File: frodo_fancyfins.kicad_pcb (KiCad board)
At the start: 2 copper layers, 150 x 230 mm, 116 parts, among them J1 Molex MicroFit 2x3, J2 Molex MicroFit 2x3, J3 U.FL, J4 SWD Header, Q1 AO3400A, U10 L78L05_SOT89, U11 L78L05_SOT89, U12 L78L05_SOT89, U14 INA826, U15 AZ1117-5.0, U16 AZ1117-5.0, U17 W25Q128JVP, U18 AS321KTR-G1, U19 INA826, U2 MCP2562-E-SN, U3 AZ1117-3.3, U4 STM32F103RCTx, U5 L78L05_SOT89, U6 L78L05_SOT89, U7 L78L05_SOT89, U8 L78L05_SOT89, U9 L78L05_SOT89, Y1 8MHz 12pF

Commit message: PCB Layout (traces, edge cuts, silk screen, 3d models)
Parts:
- J1: moved to B.Cu
- J2: moved to F.Cu
- moved J2 14.0 mm to (36.0, 287.5), turned to 0 degrees
- moved J1 12.4 mm to (36.0, 301.5), turned to 0 degrees
- moved R15 10.9 mm to (129.4, 197.7)
- moved R14 10.9 mm to (129.4, 200.2)
- moved U18 10.9 mm to (132.7, 199.4)
- moved J4 9.71 mm to (36.7, 307.5)
- moved R2 9.10 mm to (89.0, 220.6), turned to 0 degrees
- moved U17 6.51 mm to (95.5, 204.7), turned to 180 degrees
- moved C43 5.86 mm to (90.5, 207.2), turned to 90 degrees
- moved C13 2.00 mm to (69.0, 207.0)
- moved C14 2.00 mm to (69.0, 203.0)
- moved C39 2.00 mm to (52.0, 207.0)
- moved C40 2.00 mm to (52.0, 211.0)
- moved C41 2.00 mm to (52.0, 215.0)
- moved C42 2.00 mm to (52.0, 203.0)
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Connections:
- J4 pad 1: +3V3 -> +3.3V
- U2 pad 5: +3V3 -> +3.3V
- U4 pad 14: VDsense -> unconnected-(U4-PA0-Pad14)
- U4 pad 17: unconnected-(U4-PA3-Pad17) -> DIO1_RADIO
- U4 pad 20: SPI_CS_RADIO -> DIO3_RADIO
- U4 pad 24: unconnected-(U4-PC4-Pad24) -> SPI_CS_RADIO
- U4 pad 27: unconnected-(U4-PB1-Pad27) -> VDsense
- U4 pad 33: SPI_CS_FLASH -> unconnected-(U4-PB12-Pad33)
- U4 pad 37: unconnected-(U4-PC6-Pad37) -> SPI_CS_FLASH
- U4 pad 51: DIO1_RADIO -> unconnected-(U4-PC10-Pad51)
- U4 pad 52: DIO3_RADIO -> unconnected-(U4-PC11-Pad52)
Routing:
- net +3.3VA: track 0.00 -> 582.7 mm, vias 0 -> 8
- net /strain_gauge0/SG_GND: track 0.00 -> 394.3 mm
- net +3.3V: track 0.00 -> 357.5 mm, vias 0 -> 10
- net GND: track 4.00 -> 319.5 mm, vias 0 -> 267
- net VD: track 0.00 -> 259.2 mm
- net CAN-: track 0.00 -> 240.1 mm
- net CAN+: track 0.00 -> 232.4 mm, vias 0 -> 2
- net SG_REF: track 0.00 -> 231.0 mm, vias 0 -> 3
- net LED_Signal: track 0.00 -> 214.8 mm, vias 0 -> 4
- net VDC: track 0.00 -> 206.8 mm
- net +VSW: track 0.00 -> 164.8 mm
- net SWDIO: track 0.00 -> 157.2 mm
- net SWCLK: track 0.00 -> 151.1 mm
- net VDsense: track 0.00 -> 133.4 mm
- net SG_VOUT0: track 0.00 -> 130.8 mm, vias 0 -> 2
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- added copper zone on B.Cu, net +VSW
- added copper zone on B.Cu, net VDC
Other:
- board size 150 x 230 mm -> 170 x 240 mm

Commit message: Minor changes for ordering
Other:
- outline, holes or cut-outs redrawn
- board text added: "FRoDO Fancy Fins"
- board text added: "JLCJLCJLCJLC"
- board text added: "rev 0"
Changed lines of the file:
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@@
         (effects (font (size 1 1) (thickness 0.15)))
     )
-    (fp_text value "SWD Header" (at 0 9.95 90) (layer "F.Fab")
+    (fp_text value "SWD Header" (at 0 9.95 90) (layer "F.Fab") hide
         (effects (font (size 1 1) (thickness 0.15)))
     )
-    (fp_text user "${REFERENCE}" (at 0 3.81) (layer "F.Fab")
+    (fp_text user "${REFERENCE}" (at 0 3.81) (layer "F.Fab") hide
         (effects (font (size 1 1) (thickness 0.15)))
     )
@@
   (gr_line (start 50.5 309.5) (end 50.5 80.5)
     (stroke (width 0.15) (type dash)) (layer "F.SilkS"))
-  (gr_poly locked
+  (gr_poly
     (pts
       (xy 50 70)
@@
       (xy 48.5 70)
       (xy 35 70)
-      (xy 35 260)
-      (xy 30 270)
+      (xy 35 270)
+      (xy 30 280)
       (xy 30 310)
       (xy 50 310)
@@
     )
     (stroke (width 0.2) (type solid)) (fill none) (layer "Edge.Cuts"))
+  (gr_text "JLCJLCJLCJLC" (at 41.3 256.3 90) (layer "F.SilkS")
+    (effects (font (size 1 1) (thickness 0.15)) (justify left bottom))
+  )
+  (gr_text "rev 0\n" (at 44 238.8 90) (layer "F.SilkS")
+    (effects (font (size 1 1) (thickness 0.15)) (justify left bottom))
+  )
+  (gr_text "FRoDO\nFancy Fins" (at 42 239 90) (layer "F.SilkS")
+    (effects (font (size 1.5 1.5) (thickness 0.3) bold) (justify left bottom))
+  )
   (segment (start 166.0375 221.3) (end 166.0375 222.9875) (width 1.23) (layer "F.Cu") (net 1))
   (segment (start 166 221.2625) (end 166.0375 221.3) (width 1.23) (layer "F.Cu") (net 1))

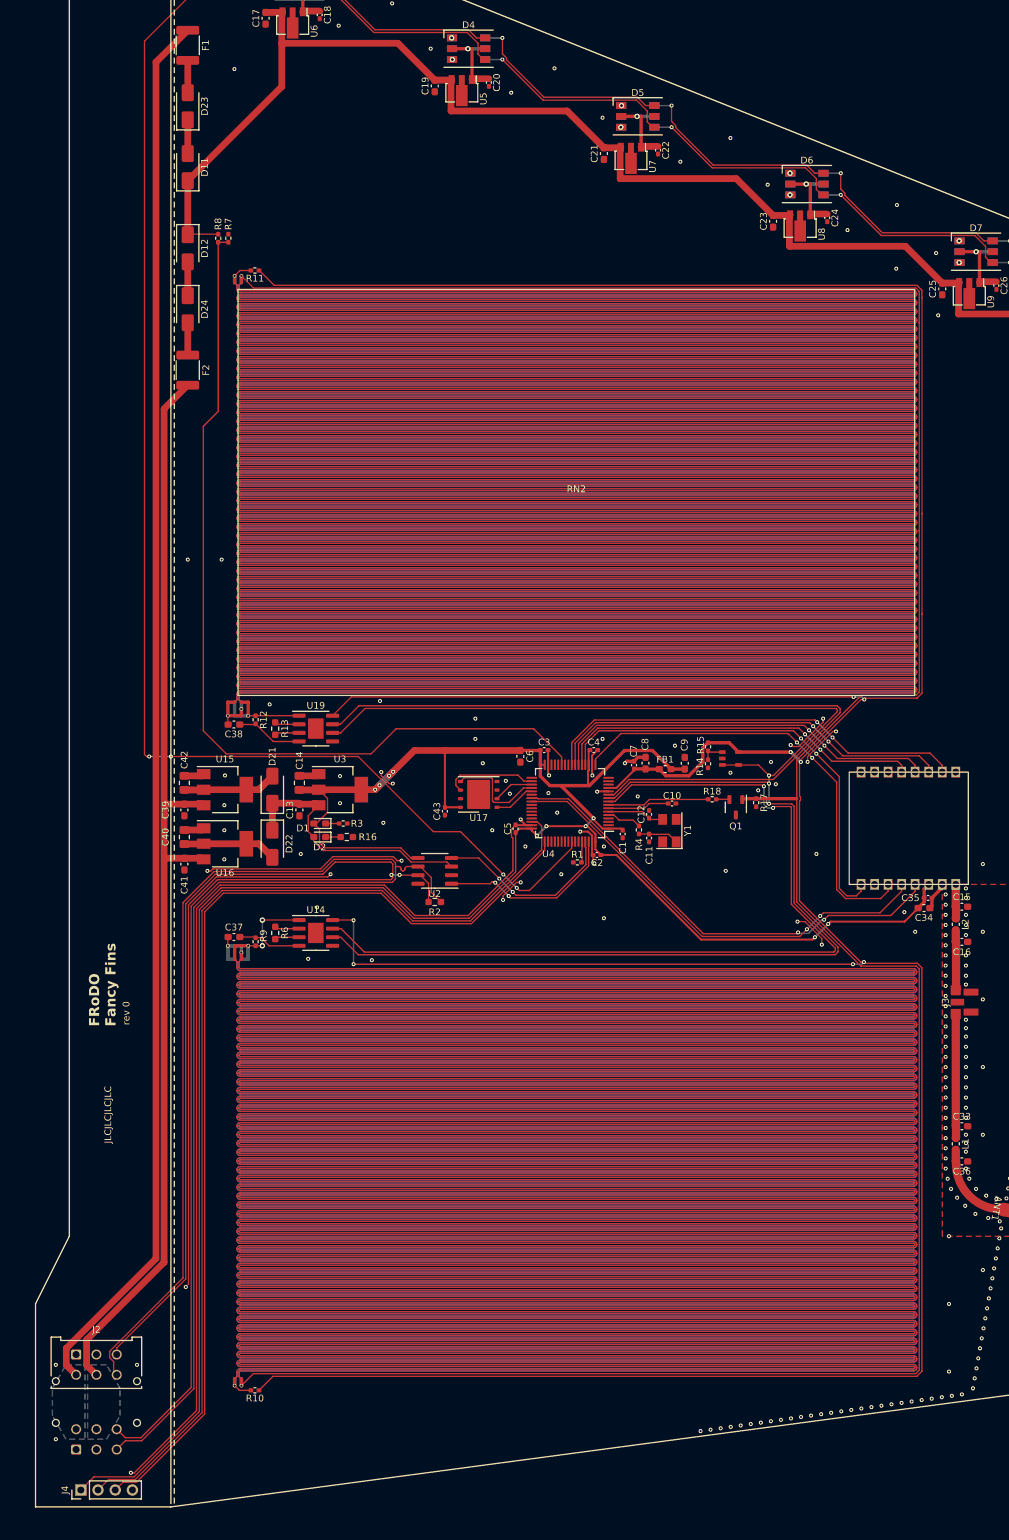
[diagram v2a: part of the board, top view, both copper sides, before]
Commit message: implement changes from rev 0 to rev 1
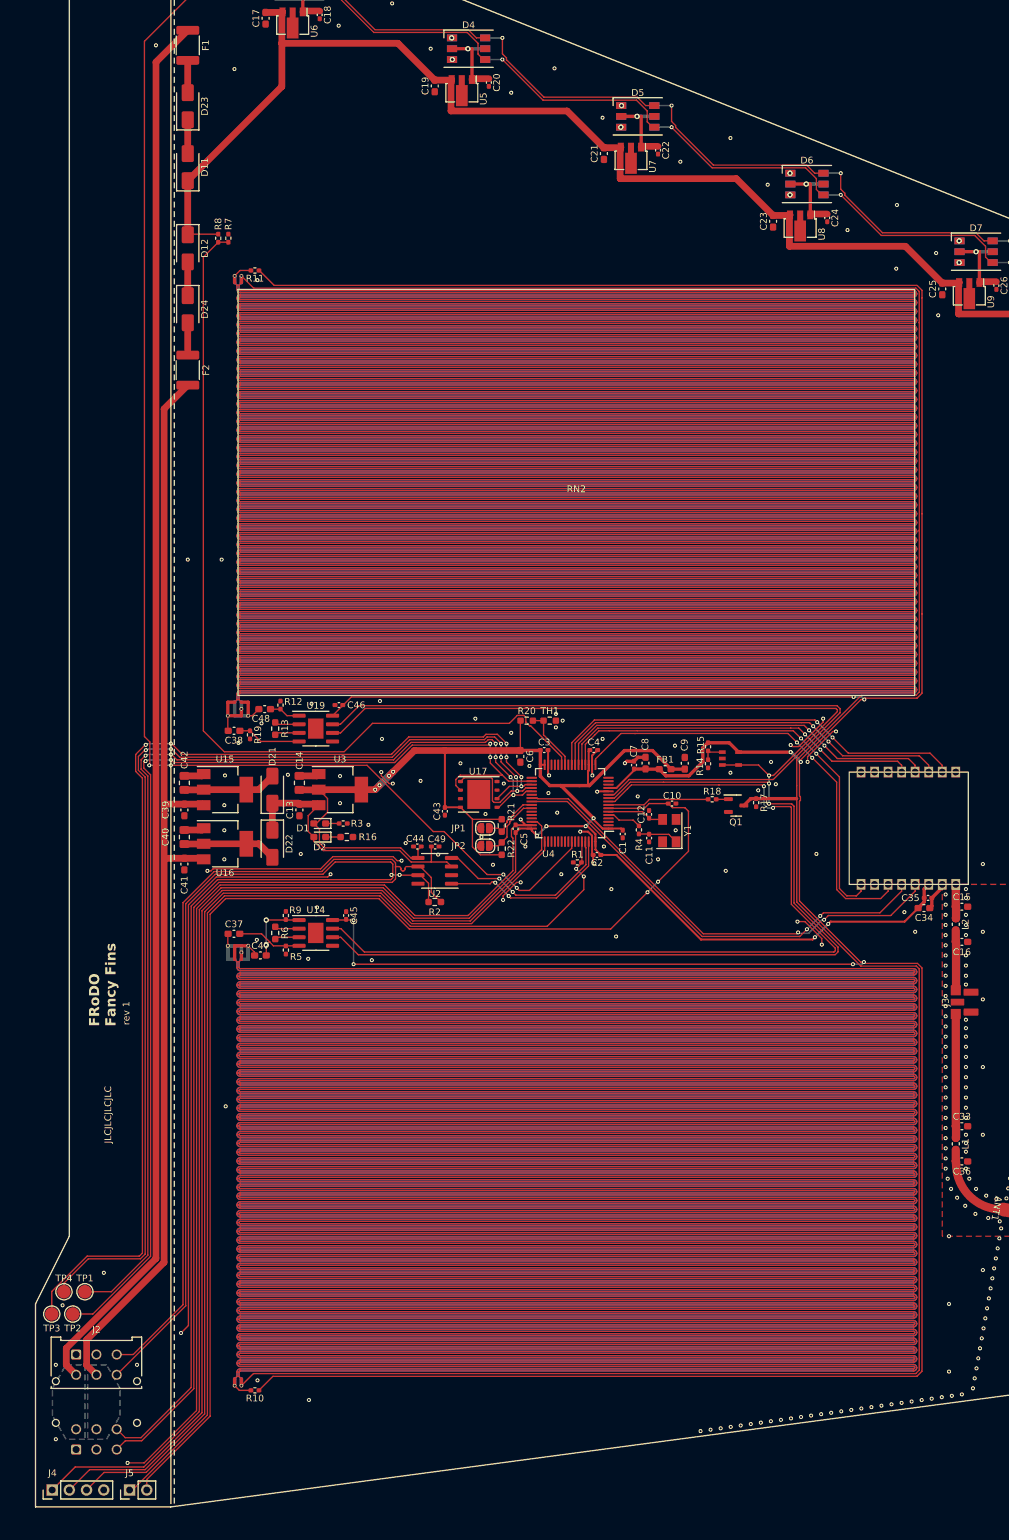
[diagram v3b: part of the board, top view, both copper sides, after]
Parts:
- added C44: 100n, Capacitor_SMD:C_0402_1005Metric_Pad0.74x0.62mm_HandSolder, F.Cu at (86.4, 212.4)
- added C45: 100n, Capacitor_SMD:C_0402_1005Metric_Pad0.74x0.62mm_HandSolder, F.Cu at (75.9, 222.6)
- added C46: 100n, Capacitor_SMD:C_0402_1005Metric_Pad0.74x0.62mm_HandSolder, F.Cu at (74.8, 191.5)
- added C47: 2u2, Capacitor_SMD:C_0603_1608Metric_Pad1.08x0.95mm_HandSolder, F.Cu at (63.2, 228.5)
- added C48: 2u2, Capacitor_SMD:C_0603_1608Metric_Pad1.08x0.95mm_HandSolder, F.Cu at (63.9, 192.1)
- added C49: 100n, Capacitor_SMD:C_0402_1005Metric_Pad0.74x0.62mm_HandSolder, F.Cu at (89.1, 212.4)
- added J5: CFG Header, Connector_PinHeader_2.54mm:PinHeader_1x02_P2.54mm_Vertical, F.Cu at (43.9, 307.5)
- added JP1: CAN ADDR 0, Jumper:SolderJumper-2_P1.3mm_Open_RoundedPad1.0x1.5mm, F.Cu at (96.5, 209.7)
- added JP2: CAN ADDR 1, Jumper:SolderJumper-2_P1.3mm_Open_RoundedPad1.0x1.5mm, F.Cu at (96.5, 212.3)
- added R19: 100k, Resistor_SMD:R_0402_1005Metric_Pad0.72x0.64mm_HandSolder, F.Cu at (61.7, 195.9)
- added R20: 10k, Resistor_SMD:R_0603_1608Metric_Pad0.98x0.95mm_HandSolder, F.Cu at (102.6, 193.8)
- added R21: 10k, Resistor_SMD:R_0603_1608Metric_Pad0.98x0.95mm_HandSolder, F.Cu at (98.9, 209.3)
- added R22: 10k, Resistor_SMD:R_0603_1608Metric_Pad0.98x0.95mm_HandSolder, F.Cu at (98.9, 212.7)
- added R5: 100k, Resistor_SMD:R_0402_1005Metric_Pad0.72x0.64mm_HandSolder, F.Cu at (67.0, 227.7)
- added TH1: 10k, Resistor_SMD:R_0603_1608Metric_Pad0.98x0.95mm_HandSolder, F.Cu at (106.0, 193.8)
- added TP1: CS, TestPoint:TestPoint_Pad_D2.0mm, F.Cu at (37.3, 278.2)
- added TP2: SCK, TestPoint:TestPoint_Pad_D2.0mm, F.Cu at (35.5, 281.5)
- added TP3: MISO, TestPoint:TestPoint_Pad_D2.0mm, F.Cu at (32.4, 281.5)
- added TP4: MOSI, TestPoint:TestPoint_Pad_D2.0mm, F.Cu at (34.2, 278.2)
- R13, R6: value 470 -> DNP
- moved R9 5.92 mm to (67.0, 222.6)
- moved R12 4.27 mm to (66.2, 191.5), turned to 90 degrees
- moved J4 4.24 mm to (32.5, 307.5)
- moved C38 0.92 mm to (59.3, 195.3)
- moved C37 0.48 mm to (59.3, 225.3)
- moved Q1 0.25 mm to (133.5, 206.3), turned to 0 degrees
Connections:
- net /BOOT0 renamed BOOT0
- net /NRST renamed NRST
- J2 pad 3: CAN+ -> CAN-
- J2 pad 6: CAN- -> CAN+
- Q1 pad 1: /strain_gauge0/SG_GND -> Net-(Q1-G)
- Q1 pad 2: Net-(Q1-G) -> GND
- Q1 pad 3: GND -> /strain_gauge0/SG_GND
- R12 pad 1: Net-(RN2-V2) -> Net-(U19--IN)
- R12 pad 2: Net-(U19-+IN) -> GND
- R9 pad 1: Net-(RN1-V2) -> Net-(U14--IN)
- R9 pad 2: Net-(U14-+IN) -> GND
- U14 pad 1: Net-(RN1-V2) -> Net-(U14--IN)
- U19 pad 1: Net-(RN2-V2) -> Net-(U19--IN)
- U4 pad 26: unconnected-(U4-PB0-Pad26) -> TH_sense
- U4 pad 41: unconnected-(U4-PA8-Pad41) -> CAN_ADDR0
- U4 pad 42: unconnected-(U4-PA9-Pad42) -> CAN_ADDR1
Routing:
- net NRST: track 9.12 -> 185.8 mm, vias 0 -> 2
- net SPI2_MISO: track 5.99 -> 164.4 mm, vias 0 -> 6
- net BOOT0: track 3.15 -> 159.0 mm, vias 0 -> 2
- net SPI2_MOSI: track 15.0 -> 168.2 mm, vias 0 -> 6
- net SPI_CS_FLASH: track 6.10 -> 154.5 mm, vias 0 -> 6
- net SPI2_SCK: track 13.7 -> 160.2 mm, vias 0 -> 4
- net +3.3V: track 357.5 -> 383.8 mm
- net Net-(U14--IN): track 0.00 -> 10.1 mm, vias 0 -> 2
- net CAN_ADDR1: track 0.00 -> 9.60 mm
- net Net-(RN1-V2): track 11.3 -> 1.82 mm, vias 2 -> 0
- net TH_sense: track 0.00 -> 9.42 mm
- net CAN_ADDR0: track 0.00 -> 8.54 mm
- net GND: track 319.5 -> 326.5 mm, vias 267 -> 290
- net Net-(RN2-V2): track 7.53 -> 1.98 mm
- net Net-(U19--IN): track 0.00 -> 4.64 mm
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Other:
- board text added: "rev 1"
- board text removed: "rev 0"

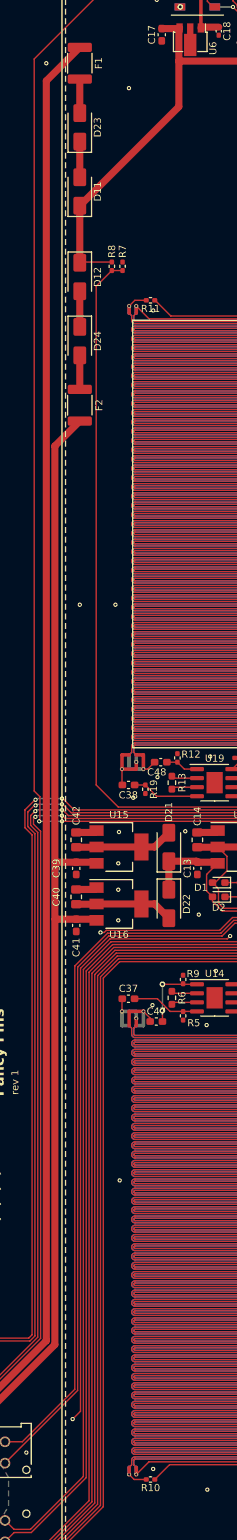
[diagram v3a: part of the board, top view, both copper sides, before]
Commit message: add LCSC part numbers, tweak some footprints
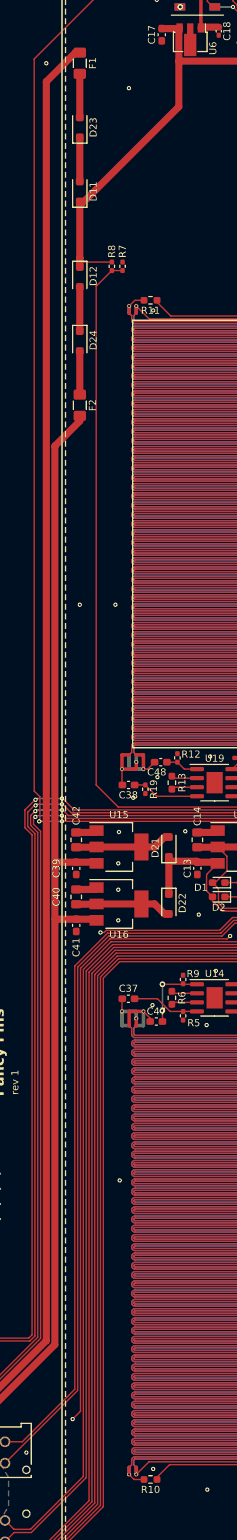
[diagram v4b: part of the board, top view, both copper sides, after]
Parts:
- C17, C19, C21, C23, C25, C27, C29, C31: value 330n -> 470
- D1: value green -> yellow
- D11, D12, D21, D22, D23, D24: footprint Diode_SMD:D_SMA -> Diode_SMD:D_SOD-123F
- F1, F2: footprint Fuse:Fuse_1812_4532Metric_Pad1.30x3.40mm_HandSolder -> Fuse:Fuse_1206_3216Metric_Pad1.42x1.75mm_HandSolder
- R10, R11: footprint Resistor_SMD:R_0402_1005Metric_Pad0.72x0.64mm_HandSolder -> Resistor_SMD:R_0603_1608Metric_Pad0.98x0.95mm_HandSolder
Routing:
- net VD: track 259.2 -> 261.1 mm
- net Net-(D23-A): track 4.78 -> 6.11 mm
- net Net-(D24-A): track 4.78 -> 6.11 mm
- net Net-(D12-A): track 5.00 -> 6.20 mm
- net Net-(D11-A): track 5.00 -> 6.20 mm
- net +5V: track 41.5 -> 42.7 mm
- net +VSW: track 164.8 -> 165.5 mm
